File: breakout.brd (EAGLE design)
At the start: 55.9 x 12.7 mm, 8 parts, among them P1@1 M01PTH, P1@2 M01PTH, P2@1 M01PTH, P2@2 M01PTH, P3@1 M01PTH, P3@2 M01PTH

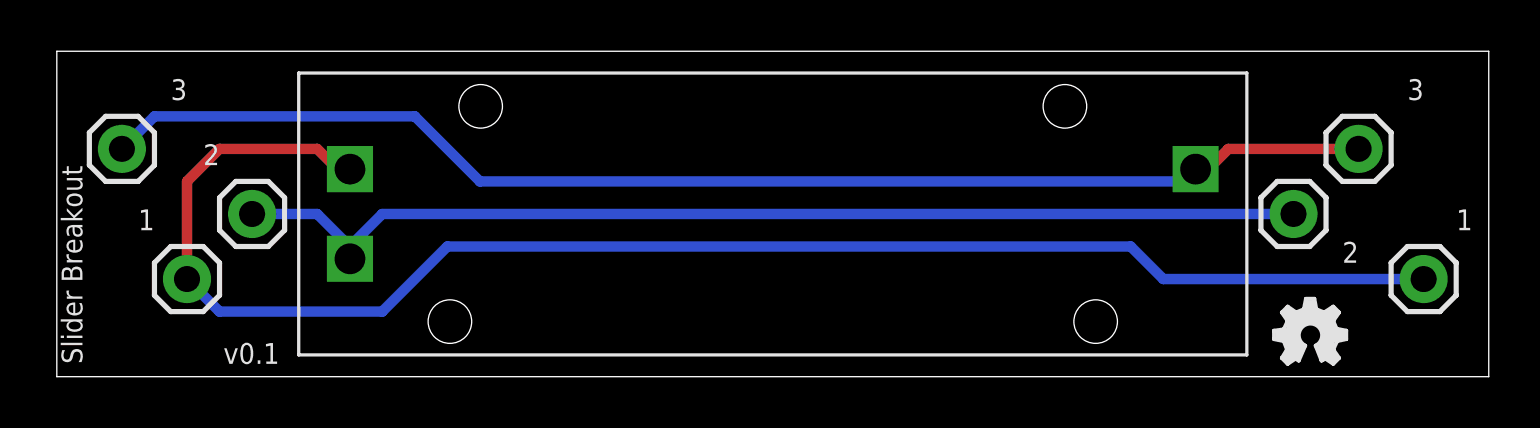
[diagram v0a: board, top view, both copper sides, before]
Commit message: adding tolerance to slider tab drill holes
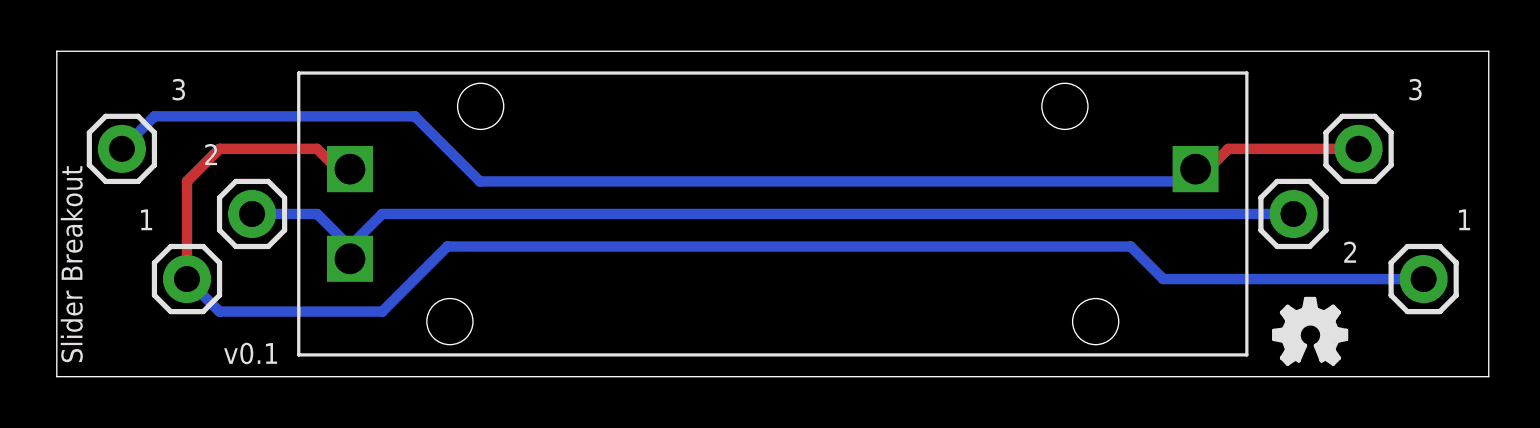
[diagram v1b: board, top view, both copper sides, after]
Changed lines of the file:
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@@
 </elements>
 <signals>
-<signal name="N$1">
+<signal name="N$2">
+<contactref element="P2@1" pad="1"/>
+<contactref element="U$1" pad="P$2"/>
+<contactref element="P2@2" pad="1"/>
+<wire x1="7.62" y1="6.35" x2="10.16" y2="6.35" width="0.4064" layer="16"/>
+<wire x1="10.16" y1="6.35" x2="11.43" y2="5.08" width="0.4064" layer="16"/>
+<wire x1="11.43" y1="5.08" x2="12.7" y2="6.35" width="0.4064" layer="16"/>
+<wire x1="12.7" y1="6.35" x2="48.26" y2="6.35" width="0.4064" layer="16"/>
+<wire x1="11.43" y1="5.08" x2="11.44" y2="4.6" width="0" layer="19" extent="16-16"/>
+</signal>
+<signal name="N$3">
+<contactref element="U$1" pad="P$3"/>
 <contactref element="P3@1" pad="1"/>
-<contactref element="U$1" pad="P$3"/>
 <contactref element="P3@2" pad="1"/>
-<wire x1="3.81" y1="10.16" x2="2.54" y2="8.89" width="0.4064" layer="16"/>
-<wire x1="13.97" y1="10.16" x2="3.81" y2="10.16" width="0.4064" layer="16"/>
-<wire x1="16.51" y1="7.62" x2="13.97" y2="10.16" width="0.4064" layer="16"/>
-<wire x1="44.45" y1="7.62" x2="16.51" y2="7.62" width="0.4064" layer="16"/>
-<wire x1="44.44" y1="8.1" x2="44.44" y2="7.63" width="0.4064" layer="16"/>
-<wire x1="44.44" y1="7.63" x2="44.45" y2="7.62" width="0.4064" layer="16"/>
+<wire x1="2.54" y1="8.89" x2="3.81" y2="10.16" width="0.4064" layer="16"/>
+<wire x1="3.81" y1="10.16" x2="13.97" y2="10.16" width="0.4064" layer="16"/>
+<wire x1="13.97" y1="10.16" x2="16.51" y2="7.62" width="0.4064" layer="16"/>
+<wire x1="16.51" y1="7.62" x2="43.96" y2="7.62" width="0.4064" layer="16"/>
+<wire x1="43.96" y1="7.62" x2="44.44" y2="8.1" width="0.4064" layer="16"/>
 <wire x1="44.44" y1="8.1" x2="44.93" y2="8.1" width="0.4064" layer="1"/>
 <wire x1="44.93" y1="8.1" x2="45.72" y2="8.89" width="0.4064" layer="1"/>
 <wire x1="45.72" y1="8.89" x2="50.8" y2="8.89" width="0.4064" layer="1"/>
 </signal>
-<signal name="N$2">
-<contactref element="P2@1" pad="1"/>
-<contactref element="U$1" pad="P$2"/>
-<contactref element="P2@2" pad="1"/>
-<wire x1="10.16" y1="6.35" x2="11.43" y2="5.08" width="0.4064" layer="16"/>
-<wire x1="7.62" y1="6.35" x2="10.16" y2="6.35" width="0.4064" layer="16"/>
-<wire x1="11.43" y1="5.08" x2="11.44" y2="4.6" width="0.4064" layer="16"/>
-<wire x1="11.43" y1="5.08" x2="12.7" y2="6.35" width="0.4064" layer="16"/>
-<wire x1="12.7" y1="6.35" x2="48.26" y2="6.35" width="0.4064" layer="16"/>
-</signal>
-<signal name="N$3">
+<signal name="N$4">
+<contactref element="U$1" pad="P$1"/>
 <contactref element="P1@1" pad="1"/>
-<contactref element="U$1" pad="P$1"/>
 <contactref element="P1@2" pad="1"/>
 <wire x1="5.08" y1="3.81" x2="6.35" y2="2.54" width="0.4064" layer="16"/>
